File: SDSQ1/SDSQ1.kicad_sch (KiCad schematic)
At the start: 21 parts, among them Q1 NPN, Q2 NPN, U1 Opamp_Dual

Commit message: snare main drum
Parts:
- added C8, C9: 6nF, symbol Device:C
- added D4: D, symbol Device:D
- added R10: 1M, symbol Device:R_US
- added R9: 500, symbol Device:R_US
- added U2: Opamp_Dual, symbol Device:Opamp_Dual
- C1, C2: value 1uF -> 683
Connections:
- net GND: now also R9.1
- net SD: now also U2.3 (+)
- new net: C8.2, C9.1, R9.2
- new net: C9.2, D4.2 (A), R10.1, U2.1
- new net: C8.1, R10.2, U2.2 (-)
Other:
- note added: "Snare Drum"
- note added: "Target freq: 110Hz Target decay time: 100ms .07(pi(110)) = Q Target Q = 25"

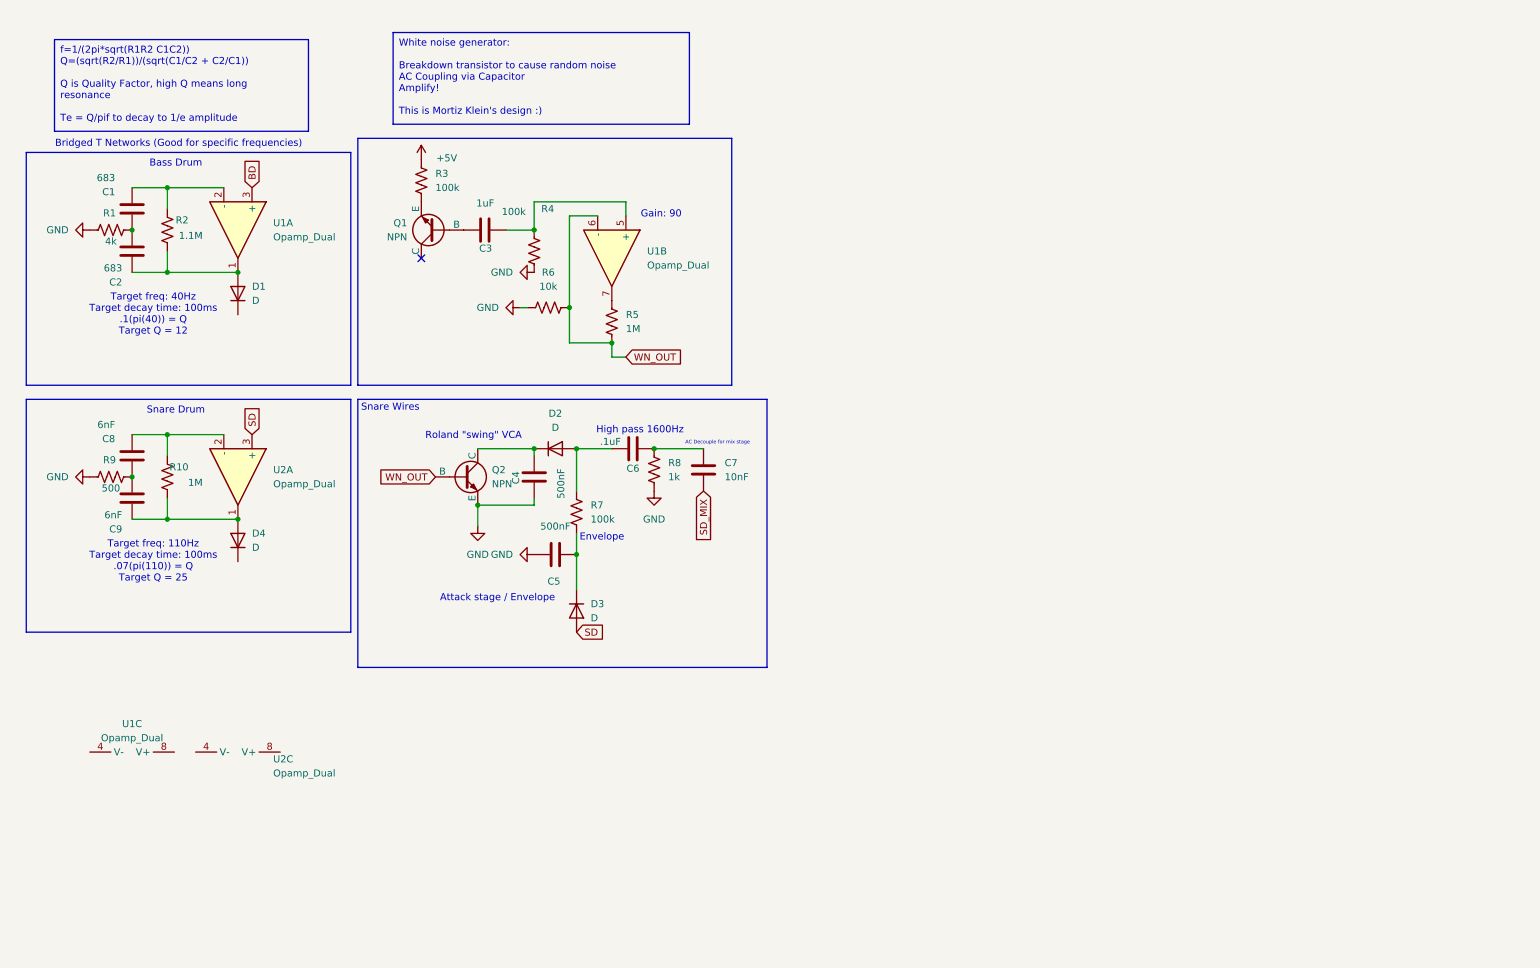
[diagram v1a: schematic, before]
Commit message: added hats
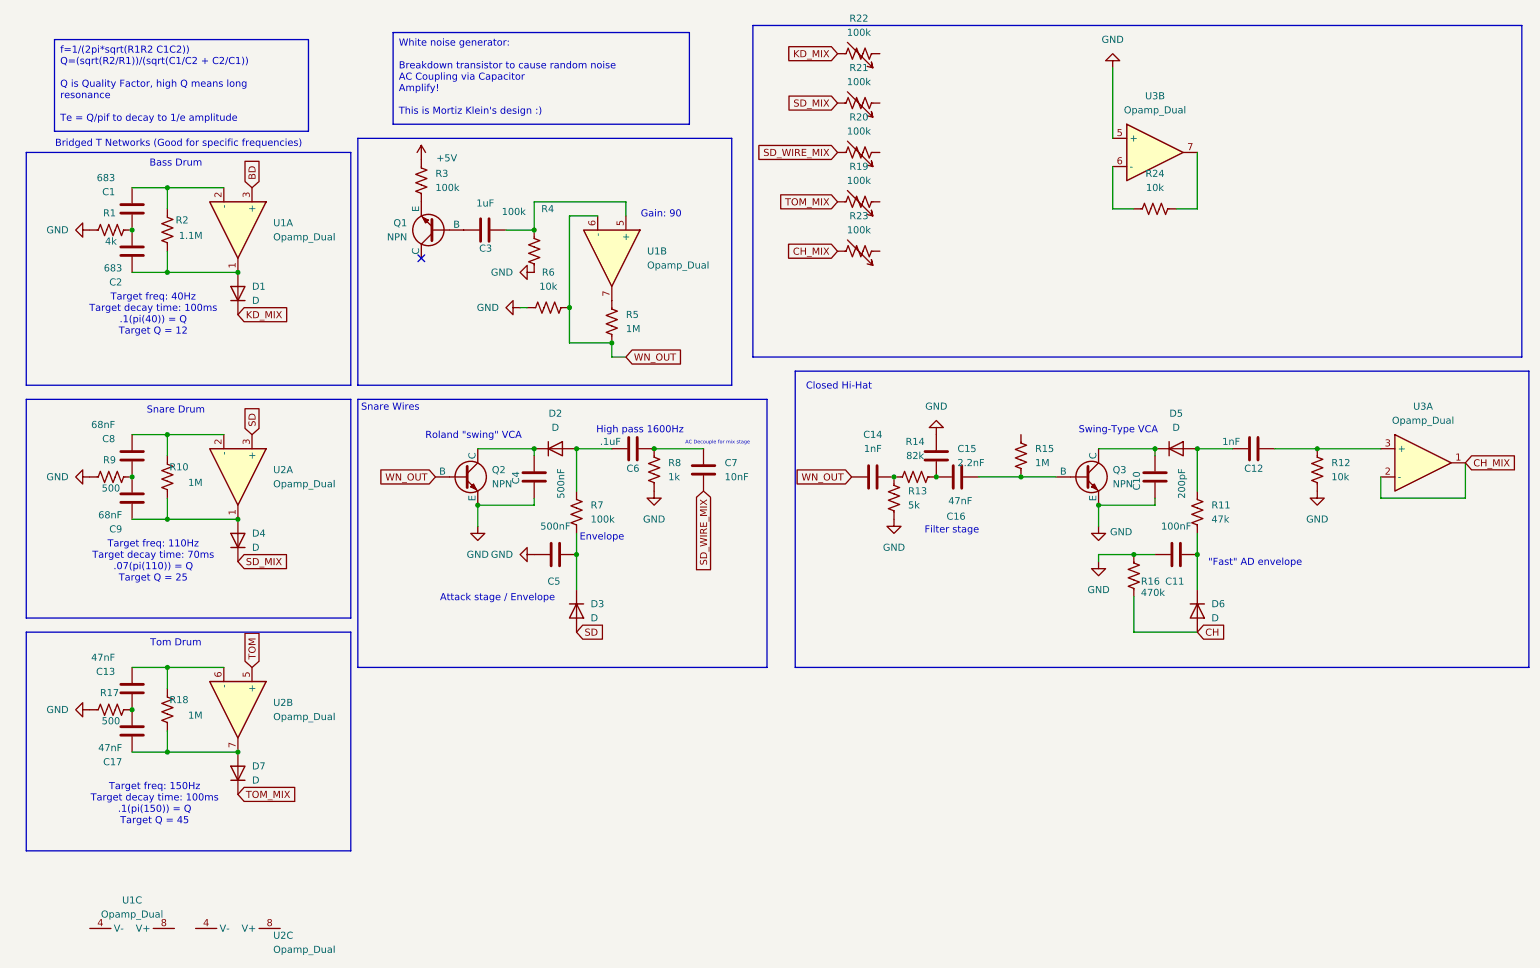
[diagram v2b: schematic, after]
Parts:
- added C10: 200pF, symbol Device:C
- added C11: 100nF, symbol Device:C
- added C12, C14: 1nF, symbol Device:C
- added C13, C16, C17: 47nF, symbol Device:C
- added C15: 2.2nF, symbol Device:C
- added D5, D6, D7: D, symbol Device:D
- added Q3: NPN, symbol Simulation_SPICE:NPN
- added R11: 47k, symbol Device:R_US
- added R12, R24: 10k, symbol Device:R_US
- added R13: 5k, symbol Device:R_US
- added R14: 82k, symbol Device:R_US
- added R15, R18: 1M, symbol Device:R_US
- added R16: 470k, symbol Device:R_US
- added R17: 500, symbol Device:R_US
- added R19, R20, R21, R22, R23: 100k, symbol Device:R_Variable_US
- added unit 2 of U2
- added U3: Opamp_Dual, symbol Device:Opamp_Dual
- C8, C9: value 6nF -> 68nF
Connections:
- net GND: now also C10.2, C11.1, C15.2, Q3.3 (E), R12.2, R13.2, R16.1, R17.1, U3.5 (+)
- net SD_MIX: now also D4.1 (K), R21.2; no longer C7.1
- net WN_OUT: now also C14.1
- net KD_MIX: now reaches D1.1 (K)
- net KD_MIX: now also R22.2
- new net: C14.2, R13.1, R14.1
- new net: C12.1, D5.2 (A), R11.1
- new net: C12.2, R12.1, U3.3 (+)
- new net: C10.1, D5.1 (K), Q3.1 (C)
- new net: C11.2, D6.1 (K), R11.2
- new net: C13.1, R18.2, U2.6 (-)
- new net: C17.2, D7.2 (A), R18.1, U2.7
- new net: R24.1, U3.6 (-)
- new net: R24.2, U3.7
- new net: C16.1, Q3.2 (B), R15.2
- new net: C15.1, C16.2, R14.2
- new net: C13.2, C17.1, R17.2
- new net CH: D6.2 (A), R16.2
- new net CH_MIX: R23.2, U3.1, U3.2 (-)
- new net SD_WIRE_MIX: C7.1, R20.2
- new net TOM: U2.5 (+)
- new net TOM_MIX: D7.1 (K), R19.2
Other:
- note added: ""Fast" AD envelope"
- note added: "Closed Hi-Hat"
- note added: "Filter stage"
- note added: "Swing-Type VCA"
- note added: "Target freq: 110Hz Target decay time: 70ms .07(pi(110)) = Q Target Q = 25"
- note added: "Target freq: 150Hz Target decay time: 100ms .1(pi(150)) = Q Target Q = 45"
- note added: "Tom Drum"
- note removed: "Target freq: 110Hz Target decay time: 100ms .07(pi(110)) = Q Target Q = 25"
- moved on the sheet: U1C, U2C

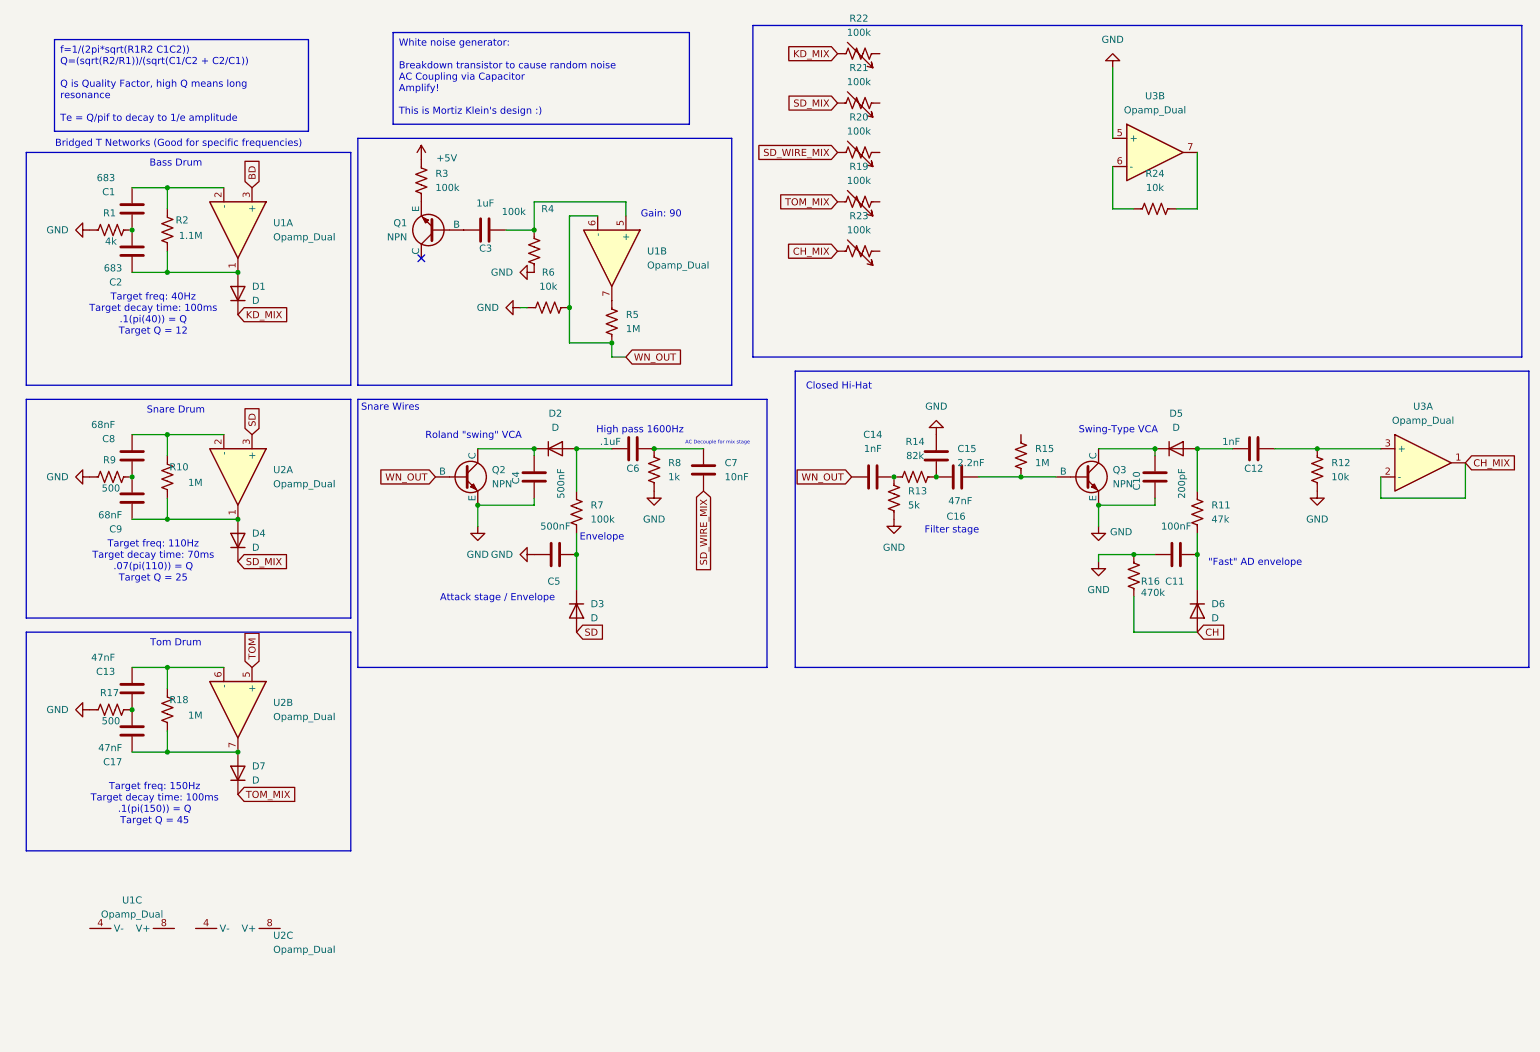
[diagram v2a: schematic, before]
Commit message: added pow management
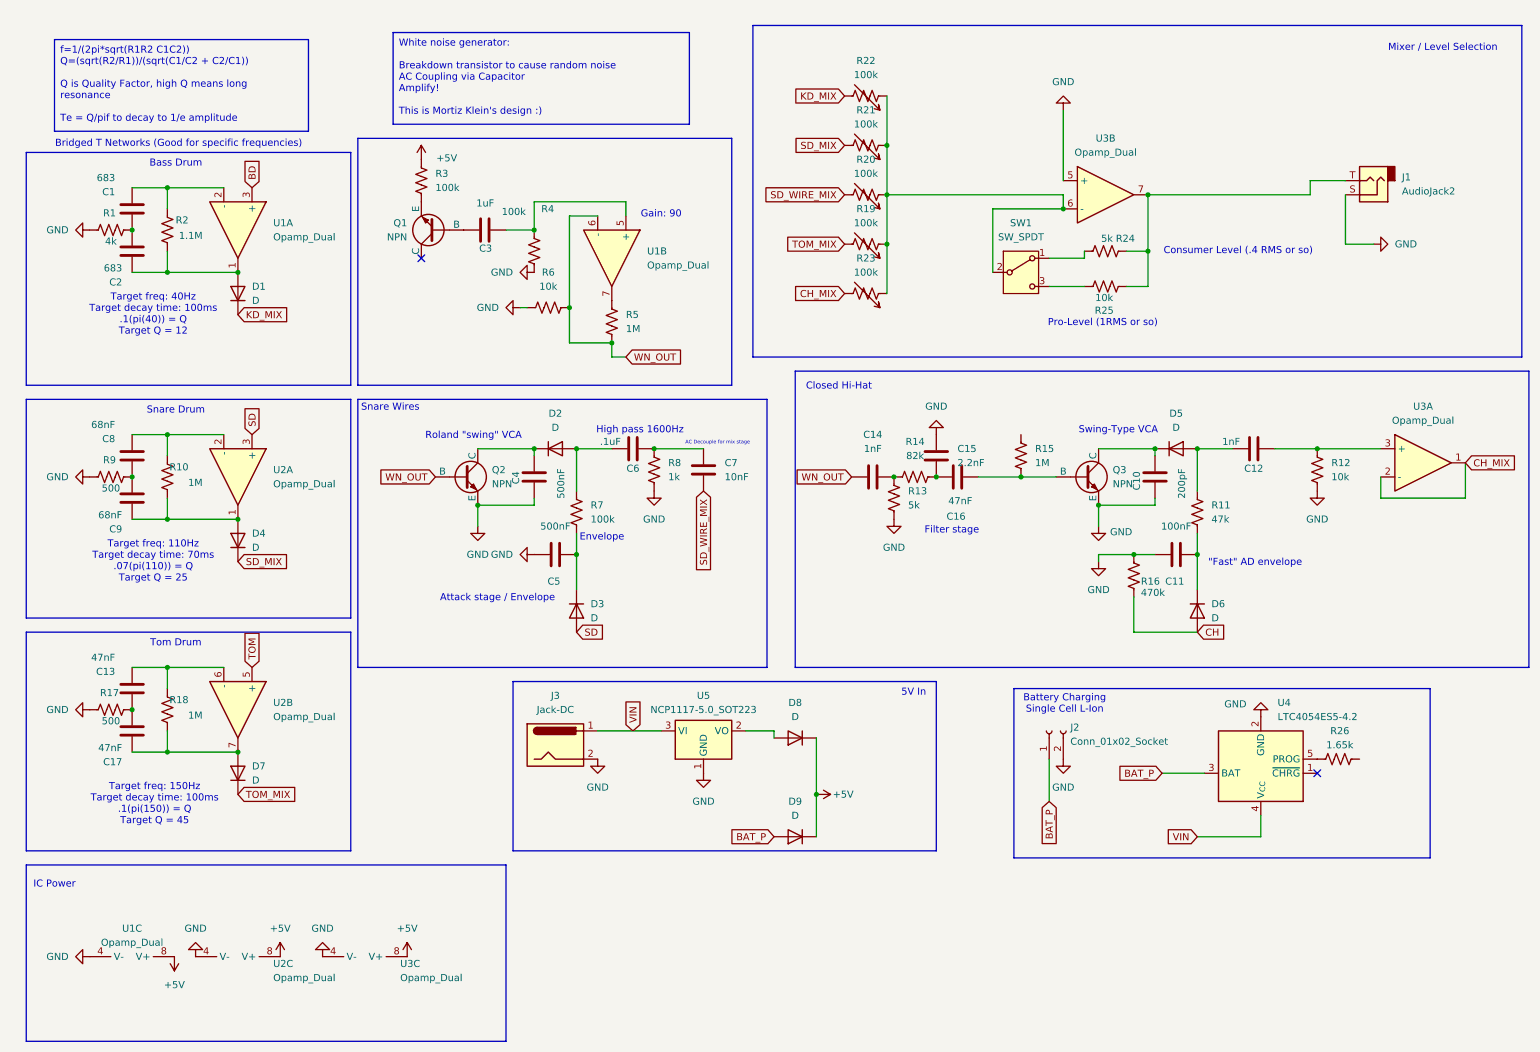
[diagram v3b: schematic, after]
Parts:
- added D8, D9: D, symbol Device:D
- added J1: AudioJack2, symbol Connector_Audio:AudioJack2
- added J2: Conn_01x02_Socket, symbol Connector:Conn_01x02_Socket
- added J3: Jack-DC, symbol Connector:Jack-DC
- added R25: 10k, symbol Device:R_US
- added R26: 1.65k, symbol Device:R_US
- added SW1: SW_SPDT, symbol Switch:SW_SPDT
- added unit 3 of U3
- added U4: LTC4054ES5-4.2, Package_TO_SOT_SMD:TSOT-23-5, symbol Battery_Management:LTC4054ES5-4.2
- added U5: NCP1117-5.0_SOT223, Package_TO_SOT_SMD:SOT-223-3_TabPin2, symbol Regulator_Linear:NCP1117-5.0_SOT223
- R24: value 10k -> 5k
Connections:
- net +5V: now also U1.8 (V+), U2.8 (V+), D8.1 (K), D9.1 (K), U3.8 (V+)
- net GND: now also U1.4 (V-), U2.4 (V-), J1.S, J2.2 (Pin_2), J3.2, U3.4 (V-), U4.2 (GND), U5.1 (GND)
- net at R20.1: now also R19.1, R21.1, R22.1, R23.1, U3.6 (-), SW1.2 (B)
- net at R24.1: now also SW1.1 (A); no longer U3.6 (-)
- net at R24.2, U3.7: now also J1.T, R25.2
- new net: R26.1, U4.5 (PROG)
- new net: D8.2 (A), U5.2 (VO)
- new net: R25.1, SW1.3 (C)
- new net BAT_P: D9.2 (A), J2.1 (Pin_1), U4.3 (BAT)
- new net VIN: J3.1, U4.4 (V_{CC}), U5.3 (VI)
- no-connect marks 1 -> 2
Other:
- note added: "5V In"
- note added: "Battery Charging Single Cell L-Ion"
- note added: "Consumer Level (.4 RMS or so)"
- note added: "IC Power"
- note added: "Mixer / Level Selection"
- note added: "Pro-Level (1RMS or so)"
- moved on the sheet: R19, R20, R21, R22, R23, R24, U1C, U2C, U3B

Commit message: fabriacation
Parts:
- removed J2: Conn_01x02_Socket, symbol Connector:Conn_01x02_Socket
- added BT1: Battery_Cell, Battery:BatteryHolder_Keystone_1042_1x18650, symbol Device:Battery_Cell
- C1, C10, C11, C12, C13, C14, C15, C16, C17, C2, C3, C4, C5, C6, C7, C8, C9: footprint (none) -> Capacitor_THT:C_Axial_L3.8mm_D2.6mm_P7.50mm_Horizontal
- D1, D2, D3, D4, D5, D6, D7, D8, D9: footprint (none) -> Diode_THT:D_A-405_P7.62mm_Horizontal
- J1: footprint (none) -> Connector_Audio:Jack_3.5mm_PJ320E_Horizontal
- J3: footprint (none) -> Connector_BarrelJack:BarrelJack_Horizontal
- Q1, Q2, Q3: footprint (none) -> Package_TO_SOT_THT:TO-92S
- R1, R10, R11, R12, R13, R14, R15, R16, R17, R18, R19, R2, R20, R21, R22, R23, R24, R25, R26, R3, R4, R5, R6, R7, R8, R9: footprint (none) -> Resistor_THT:R_Axial_DIN0204_L3.6mm_D1.6mm_P5.08mm_Vertical
- SW1: footprint (none) -> Button_Switch_THT:SW_Push_1P2T_Vertical_E-Switch_800UDP8P1A1M6
- U1, U2, U3: footprint (none) -> Package_DIP:DIP-8_W7.62mm_Socket
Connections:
- net +5V: now also R15.1
- net BAT_P: now also BT1.1 (+)
- net GND: now also R26.2, BT1.2 (-)
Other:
- added sheet sequencer (seq.kicad_sch)
